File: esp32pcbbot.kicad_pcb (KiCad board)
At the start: 2 copper layers, 110 x 170 mm, 44 parts, among them IC1 BMI055, J1 TB002-500-02BE, J2 TB002-500-02BE, J3 TB002-500-02BE, J4 215299-4, J5 SSQ-120-01-L-D, J6 215299-4, Q1 2N7002, Q2 2N7002, Q3 Q_Photo_NPN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

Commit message: ...and i sized a voltage regulator incorrectly
...goshdangit here we go again autorouting...
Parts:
- VR2: value L78M05ABDT-TR -> L7905ACD2T-TR; footprint SamacSys_Parts:L78M05ABDTTR -> SamacSys_Parts:TO254P1542X460-3N
- moved J5 12.5 mm to (114.0, 64.5)
- moved S1 10.0 mm to (65.0, 74.0)
- moved S2 10.0 mm to (115.0, 74.0)
- moved S5 9.01 mm to (104.5, 70.0)
- moved J1 3.00 mm to (141.0, 51.0)
- moved J2 3.00 mm to (39.0, 56.0)
- moved J6 2.08 mm to (48.9, 75.0)
- moved VR1 1.52 mm to (107.2, 51.5)
- moved C4 1.50 mm to (130.0, 36.5)
- moved J3 1.50 mm to (107.0, 27.5)
- moved C7 1.41 mm to (117.0, 51.0)
- moved C8 1.00 mm to (130.0, 51.0)
- moved VR2 0.67 mm to (115.0, 38.0), turned to 0 degrees
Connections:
- VR2 pad 1: VCC -> GND
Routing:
- net GND: track 593.8 -> 0.00 mm, vias 1 -> 0
- net +5V: track 347.6 -> 0.00 mm, vias 2 -> 0
- net +3V3: track 214.9 -> 0.00 mm, vias 5 -> 0
- net 10Y: track 173.0 -> 0.00 mm, vias 1 -> 0
- net 12Y: track 150.6 -> 0.00 mm, vias 2 -> 0
- net 11Y: track 142.3 -> 0.00 mm
- net BOOT: track 137.3 -> 0.00 mm, vias 2 -> 0
- net VBUS: track 134.7 -> 0.00 mm, vias 4 -> 0
- net 7A: track 124.9 -> 0.00 mm, vias 3 -> 0
- net EN: track 124.5 -> 0.00 mm, vias 3 -> 0
- net 9Y: track 113.6 -> 0.00 mm
- net M1A: track 107.6 -> 0.00 mm
- net Net-(S2-Pad2): track 106.6 -> 0.00 mm, vias 1 -> 0
- net Net-(J5-Pad15): track 103.4 -> 0.00 mm, vias 2 -> 0
- net 10A: track 98.5 -> 0.00 mm, vias 5 -> 0
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
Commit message: work pls work pls i beg u to finally work
the ground thingy has been updated
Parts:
- moved C7 1.41 mm to (118.0, 52.0)
- moved C8 1.00 mm to (130.0, 52.0)
- moved VR2 1.00 mm to (115.0, 39.0)
- moved C4 0.50 mm to (130.0, 37.0)
- moved J3 0.50 mm to (107.0, 28.0)

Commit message: more autorouting shenanigins
please work i beg you pleaseworkpleaseworkpleasworkpleasework
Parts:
- moved Q1 5.39 mm to (61.0, 35.0)
- moved R4 4.47 mm to (61.0, 32.0)
- moved R3 3.75 mm to (60.8, 38.0)
- moved Q2 3.16 mm to (61.0, 41.0)
- moved U2 3.13 mm to (71.0, 39.9)
- moved R1 1.41 mm to (61.0, 30.0), turned to 180 degrees
- moved C3 1.00 mm to (50.0, 37.0)
- moved C5 1.00 mm to (50.0, 52.0)
- moved C6 1.00 mm to (62.0, 52.0)
- moved R2 1.00 mm to (61.0, 28.0), turned to 0 degrees
- moved USB1 1.00 mm to (71.0, 27.5)
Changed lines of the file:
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@@
   )
   (module SamacSys_Parts:EEEFK1V331P (layer F.Cu)
-    (at 62 51 180)
+    (at 62 52 180)
     (descr G)
     (tags "Capacitor Polarised")
@@
   )
   (module SamacSys_Parts:EEEFK1V331P (layer F.Cu)
-    (at 50 51 180)
+    (at 50 52 180)
     (descr G)
     (tags "Capacitor Polarised")
@@
   )
   (module SamacSys_Parts:EEEFK1V331P (layer F.Cu)
-    (at 50 36 180)
+    (at 50 37 180)
     (descr G)
     (tags "Capacitor Polarised")
@@
   )
   (module ESP32bot:USB_C_Receptacle_HRO_TYPE-C-31-M-12 (layer F.Cu)
-    (at 70 27.5 180)
+    (at 71 27.5 180)
     (descr "USB Type-C receptacle for USB 2.0 and PD, http://www.krhro.com/uploads/soft/180320/1-1P320120243.pdf")
     (tags "usb usb-c 2.0 pd")
@@
   )
   (module Package_DFN_QFN:QFN-28-1EP_5x5mm_P0.5mm_EP3.35x3.35mm (layer F.Cu)
-    (at 74 39 270)
+    (at 71 39.88 270)
     (descr "QFN, 28 Pin (http://ww1.microchip.com/downloads/en/PackagingSpec/00000049BQ.pdf#page=283), generated with kicad-footprint-generator ipc_noLead_generator.py")
     (tags "QFN NoLead")
@@
   )
   (module Resistor_SMD:R_0603_1608Metric (layer F.Cu)
-    (at 59 36)
+    (at 61 32)
     (descr "Resistor SMD 0603 (1608 Metric), square (rectangular) end terminal, IPC_7351 nominal, (Body size source: IPC-SM-782 page 72, https://www.pcb-3d.com/wordpress/wp-content/uploads/ipc-sm-782a_amendment_1_and_2.pdf), generated with kicad-footprint-generator")
     (tags resistor)
@@
   )
   (module Resistor_SMD:R_0603_1608Metric (layer F.Cu)
-    (at 64 36 180)
+    (at 60.825 38 180)
     (descr "Resistor SMD 0603 (1608 Metric), square (rectangular) end terminal, IPC_7351 nominal, (Body size source: IPC-SM-782 page 72, https://www.pcb-3d.com/wordpress/wp-content/uploads/ipc-sm-782a_amendment_1_and_2.pdf), generated with kicad-footprint-generator")
     (tags resistor)
@@
   )
   (module Resistor_SMD:R_0603_1608Metric (layer F.Cu)
-    (at 62 28 270)
+    (at 61 28)
     (descr "Resistor SMD 0603 (1608 Metric), square (rectangular) end terminal, IPC_7351 nominal, (Body size source: IPC-SM-782 page 72, https://www.pcb-3d.com/wordpress/wp-content/uploads/ipc-sm-782a_amendment_1_and_2.pdf), generated with kicad-footprint-generator")
     (tags resistor)
     (attr smd)
-    (fp_text reference R2 (at 0 -1 90) (layer F.SilkS)
-      (effects (font (size 1 1) (thickness 0.15)))
-    )
-    (fp_text value 5.11k (at 0 1.43 90) (layer F.Fab)
+    (fp_text reference R2 (at 0 -1) (layer F.SilkS)
+      (effects (font (size 1 1) (thickness 0.15)))
+    )
+    (fp_text value 5.11k (at 0 1.43) (layer F.Fab)
       (effects (font (size 1 1) (thickness 0.15)))
     )
@@
     (fp_line (start 1.48 -0.73) (end 1.48 0.73) (layer F.CrtYd) (width 0.05))
     (fp_line (start 1.48 0.73) (end -1.48 0.73) (layer F.CrtYd) (width 0.05))
-    (fp_text user %R (at -1 -1 90) (layer F.Fab)
+    (fp_text user %R (at -1 -1) (layer F.Fab)
       (effects (font (size 0.4 0.4) (thickness 0.06)))
     )
-    (pad 2 smd roundrect (at 0.825 0 270) (size 0.8 0.95) (layers F.Cu F.Paste F.Mask) (roundrect_rratio 0.25)
-      (net 2 GND))
-    (pad 1 smd roundrect (at -0.825 0 270) (size 0.8 0.95) (layers F.Cu F.Paste F.Mask) (roundrect_rratio 0.25)
+    (pad 2 smd roundrect (at 0.825 0) (size 0.8 0.95) (layers F.Cu F.Paste F.Mask) (roundrect_rratio 0.25)
+      (net 2 GND))
+    (pad 1 smd roundrect (at -0.825 0) (size 0.8 0.95) (layers F.Cu F.Paste F.Mask) (roundrect_rratio 0.25)
       (net 58 "Net-(R2-Pad1)"))
     (model ${KISYS3DMOD}/Resistor_SMD.3dshapes/R_0603_1608Metric.wrl
@@
   )
   (module Resistor_SMD:R_0603_1608Metric (layer F.Cu)
-    (at 62 31 90)
+    (at 61 30 180)
     (descr "Resistor SMD 0603 (1608 Metric), square (rectangular) end terminal, IPC_7351 nominal, (Body size source: IPC-SM-782 page 72, https://www.pcb-3d.com/wordpress/wp-content/uploads/ipc-sm-782a_amendment_1_and_2.pdf), generated with kicad-footprint-generator")
     (tags resistor)
     (attr smd)
-    (fp_text reference R1 (at 0 -1.43 90) (layer F.SilkS)
-      (effects (font (size 1 1) (thickness 0.15)))
-    )
-    (fp_text value 5.11k (at 0 1.43 90) (layer F.Fab)
+    (fp_text reference R1 (at 0 -1.43) (layer F.SilkS)
+      (effects (font (size 1 1) (thickness 0.15)))
+    )
+    (fp_text value 5.11k (at 0 1.43) (layer F.Fab)
       (effects (font (size 1 1) (thickness 0.15)))
     )
@@
     (fp_line (start 1.48 -0.73) (end 1.48 0.73) (layer F.CrtYd) (width 0.05))
     (fp_line (start 1.48 0.73) (end -1.48 0.73) (layer F.CrtYd) (width 0.05))
-    (fp_text user %R (at 0 0 180) (layer F.Fab)
+    (fp_text user %R (at 0 0 270) (layer F.Fab)
       (effects (font (size 0.4 0.4) (thickness 0.06)))
     )
-    (pad 2 smd roundrect (at 0.825 0 90) (size 0.8 0.95) (layers F.Cu F.Paste F.Mask) (roundrect_rratio 0.25)
-      (net 2 GND))
-    (pad 1 smd roundrect (at -0.825 0 90) (size 0.8 0.95) (layers F.Cu F.Paste F.Mask) (roundrect_rratio 0.25)
+    (pad 2 smd roundrect (at 0.825 0 180) (size 0.8 0.95) (layers F.Cu F.Paste F.Mask) (roundrect_rratio 0.25)
+      (net 2 GND))
+    (pad 1 smd roundrect (at -0.825 0 180) (size 0.8 0.95) (layers F.Cu F.Paste F.Mask) (roundrect_rratio 0.25)
       (net 57 "Net-(R1-Pad1)"))
     (model ${KISYS3DMOD}/Resistor_SMD.3dshapes/R_0603_1608Metric.wrl
@@
   )
   (module Package_TO_SOT_SMD:SOT-23 (layer F.Cu)
-    (at 64 40 270)
+    (at 61 41 270)
     (descr "SOT-23, Standard")
     (tags SOT-23)
@@
   )
   (module Package_TO_SOT_SMD:SOT-23 (layer F.Cu)
-    (at 59 40 270)
+    (at 61 35 270)
     (descr "SOT-23, Standard")
     (tags SOT-23)

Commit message: routing more
please work
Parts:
- moved Q1 2.24 mm to (59.0, 36.0)
- moved Q2 2.24 mm to (59.0, 42.0)
- moved R1 2.24 mm to (59.0, 31.0)
- moved R2 2.24 mm to (59.0, 29.0)
- moved R3 2.24 mm to (58.8, 39.0)
- moved R4 2.24 mm to (59.0, 33.0)
- moved USB1 2.00 mm to (69.0, 27.5)
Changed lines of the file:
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@@
   )
   (module ESP32bot:USB_C_Receptacle_HRO_TYPE-C-31-M-12 (layer F.Cu)
-    (at 71 27.5 180)
+    (at 69 27.5 180)
     (descr "USB Type-C receptacle for USB 2.0 and PD, http://www.krhro.com/uploads/soft/180320/1-1P320120243.pdf")
     (tags "usb usb-c 2.0 pd")
@@
   )
   (module Resistor_SMD:R_0603_1608Metric (layer F.Cu)
-    (at 61 32)
+    (at 59 33)
     (descr "Resistor SMD 0603 (1608 Metric), square (rectangular) end terminal, IPC_7351 nominal, (Body size source: IPC-SM-782 page 72, https://www.pcb-3d.com/wordpress/wp-content/uploads/ipc-sm-782a_amendment_1_and_2.pdf), generated with kicad-footprint-generator")
     (tags resistor)
@@
   )
   (module Resistor_SMD:R_0603_1608Metric (layer F.Cu)
-    (at 60.825 38 180)
+    (at 58.825 39 180)
     (descr "Resistor SMD 0603 (1608 Metric), square (rectangular) end terminal, IPC_7351 nominal, (Body size source: IPC-SM-782 page 72, https://www.pcb-3d.com/wordpress/wp-content/uploads/ipc-sm-782a_amendment_1_and_2.pdf), generated with kicad-footprint-generator")
     (tags resistor)
@@
   )
   (module Resistor_SMD:R_0603_1608Metric (layer F.Cu)
-    (at 61 28)
+    (at 59 29)
     (descr "Resistor SMD 0603 (1608 Metric), square (rectangular) end terminal, IPC_7351 nominal, (Body size source: IPC-SM-782 page 72, https://www.pcb-3d.com/wordpress/wp-content/uploads/ipc-sm-782a_amendment_1_and_2.pdf), generated with kicad-footprint-generator")
     (tags resistor)
@@
   )
   (module Resistor_SMD:R_0603_1608Metric (layer F.Cu)
-    (at 61 30 180)
+    (at 59 31 180)
     (descr "Resistor SMD 0603 (1608 Metric), square (rectangular) end terminal, IPC_7351 nominal, (Body size source: IPC-SM-782 page 72, https://www.pcb-3d.com/wordpress/wp-content/uploads/ipc-sm-782a_amendment_1_and_2.pdf), generated with kicad-footprint-generator")
     (tags resistor)
@@
   )
   (module Package_TO_SOT_SMD:SOT-23 (layer F.Cu)
-    (at 61 41 270)
+    (at 59 42 270)
     (descr "SOT-23, Standard")
     (tags SOT-23)
@@
   )
   (module Package_TO_SOT_SMD:SOT-23 (layer F.Cu)
-    (at 61 35 270)
+    (at 59 36 270)
     (descr "SOT-23, Standard")
     (tags SOT-23)

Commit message: more autorouting
lets hope this works
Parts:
- moved Q1 16.6 mm to (74.0, 43.0)
- moved Q2 16.6 mm to (74.0, 49.0)
- moved R3 16.6 mm to (73.8, 46.0)
- moved R4 16.6 mm to (74.0, 40.0)
- moved U2 6.29 mm to (65.0, 38.0)
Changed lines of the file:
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@@
   )
   (module Package_DFN_QFN:QFN-28-1EP_5x5mm_P0.5mm_EP3.35x3.35mm (layer F.Cu)
-    (at 71 39.88 270)
+    (at 65 38 270)
     (descr "QFN, 28 Pin (http://ww1.microchip.com/downloads/en/PackagingSpec/00000049BQ.pdf#page=283), generated with kicad-footprint-generator ipc_noLead_generator.py")
     (tags "QFN NoLead")
@@
   )
   (module Resistor_SMD:R_0603_1608Metric (layer F.Cu)
-    (at 59 33)
+    (at 74 40)
     (descr "Resistor SMD 0603 (1608 Metric), square (rectangular) end terminal, IPC_7351 nominal, (Body size source: IPC-SM-782 page 72, https://www.pcb-3d.com/wordpress/wp-content/uploads/ipc-sm-782a_amendment_1_and_2.pdf), generated with kicad-footprint-generator")
     (tags resistor)
@@
   )
   (module Resistor_SMD:R_0603_1608Metric (layer F.Cu)
-    (at 58.825 39 180)
+    (at 73.825 46 180)
     (descr "Resistor SMD 0603 (1608 Metric), square (rectangular) end terminal, IPC_7351 nominal, (Body size source: IPC-SM-782 page 72, https://www.pcb-3d.com/wordpress/wp-content/uploads/ipc-sm-782a_amendment_1_and_2.pdf), generated with kicad-footprint-generator")
     (tags resistor)
@@
   )
   (module Package_TO_SOT_SMD:SOT-23 (layer F.Cu)
-    (at 59 42 270)
+    (at 74 49 270)
     (descr "SOT-23, Standard")
     (tags SOT-23)
@@
   )
   (module Package_TO_SOT_SMD:SOT-23 (layer F.Cu)
-    (at 59 36 270)
+    (at 74 43 270)
     (descr "SOT-23, Standard")
     (tags SOT-23)

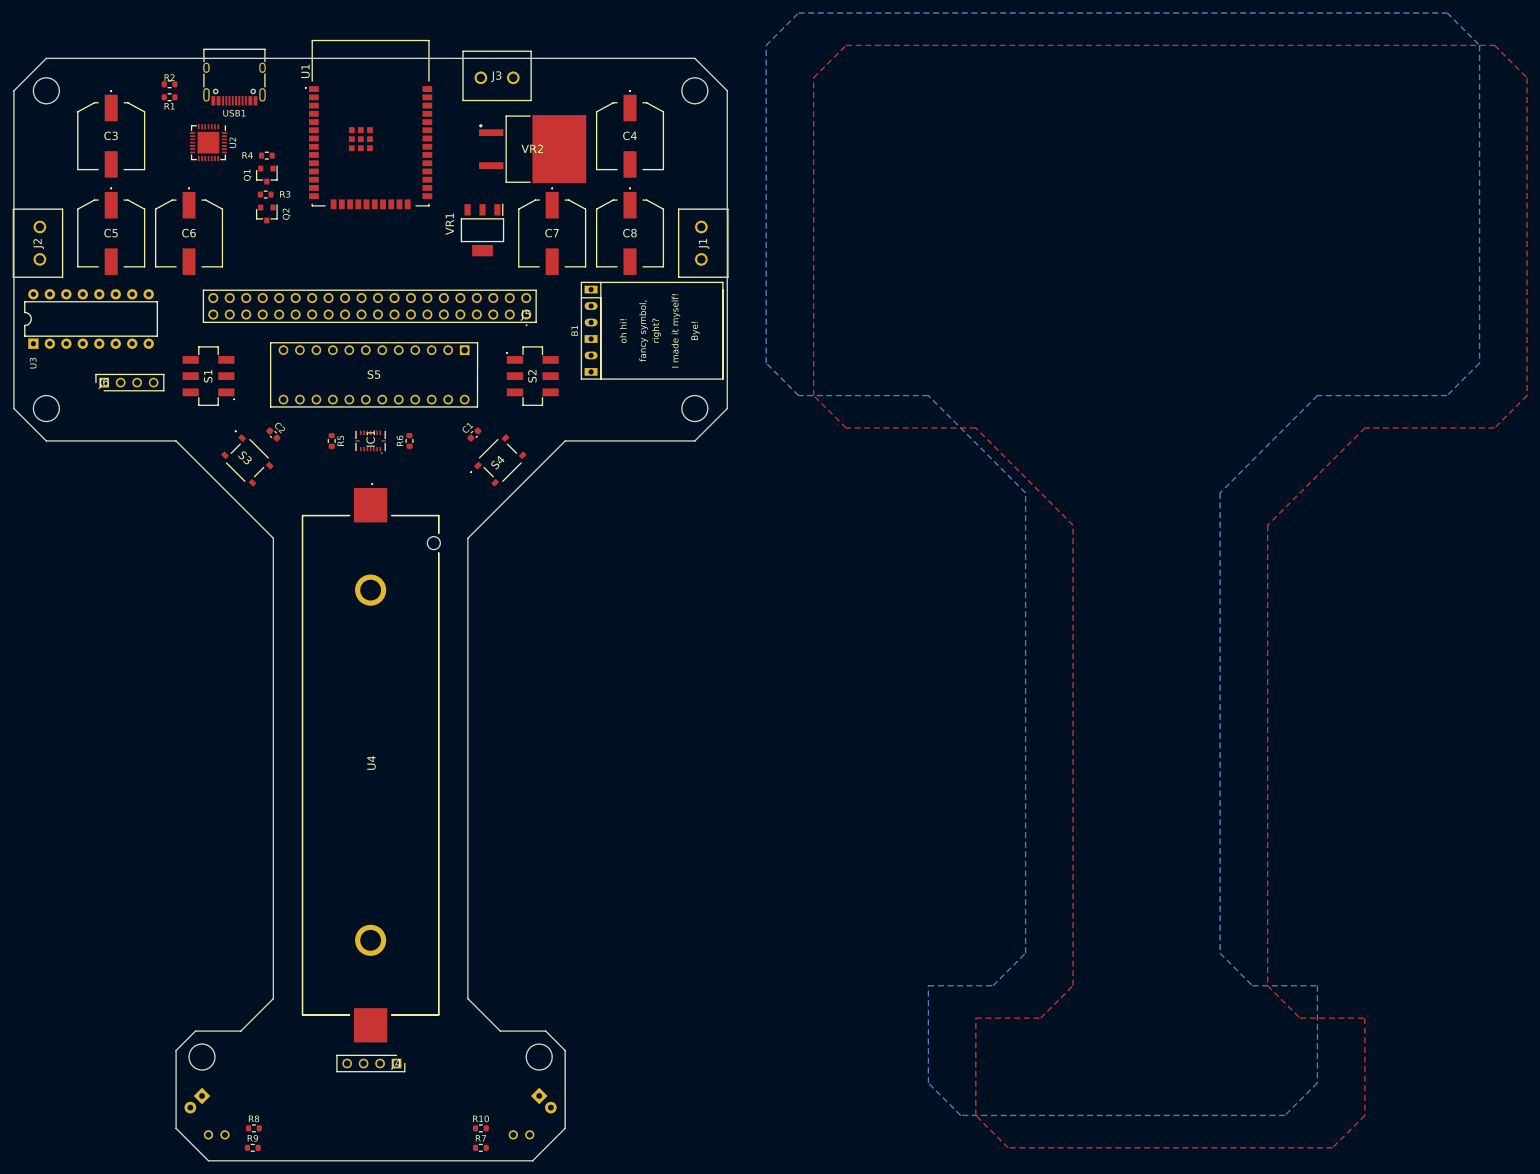
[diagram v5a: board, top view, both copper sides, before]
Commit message: more autorouting
user error last time, lets hope this one works
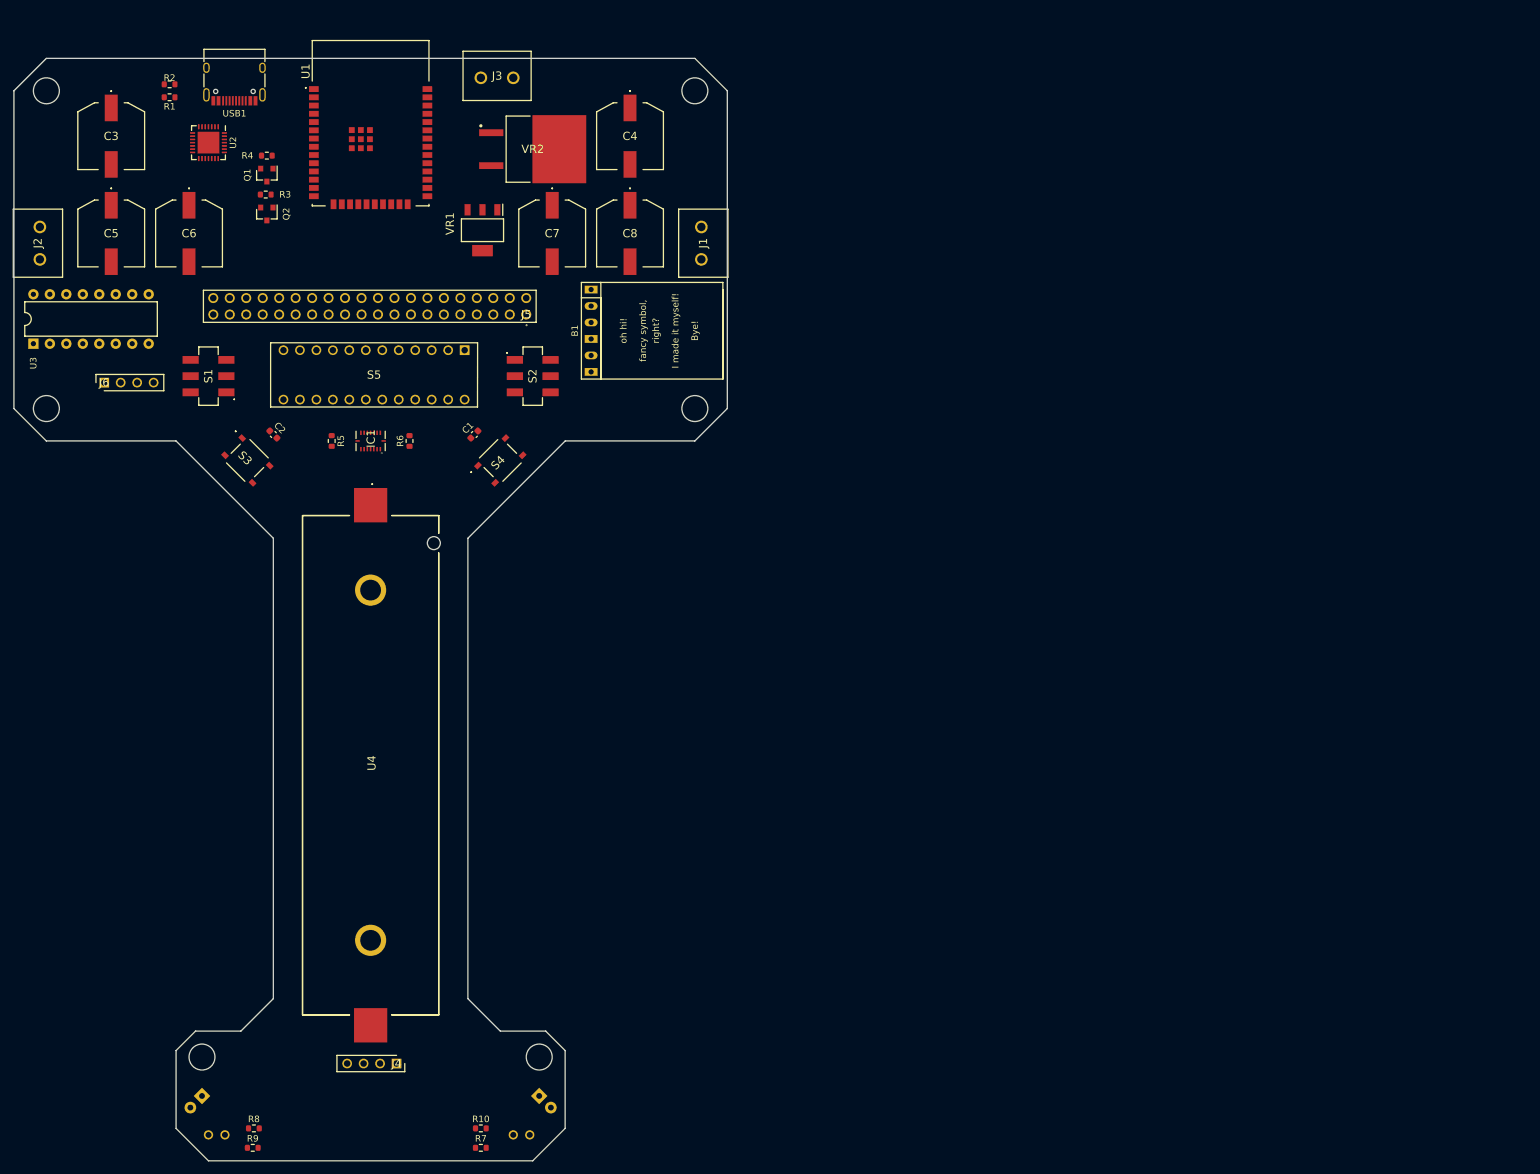
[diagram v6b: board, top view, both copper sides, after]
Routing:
- removed copper zone on B.Cu, net GND
- removed copper zone on F.Cu, net GND
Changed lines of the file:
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@@
-    )
-  )
-  (zone (net 2) (net_name GND) (layer F.Cu) (hatch edge 0.508)
-    (connect_pads (clearance 0.508))
-    (min_thickness 0.254)
-    (fill yes (arc_segments 32) (thermal_gap 0.508) (thermal_bridge_width 0.508))
-    (polygon
-      (pts
-        (xy 268.322887 28) (xy 268.322887 77) (xy 263.322887 82) (xy 243.322887 82) (xy 228.322887 97)
-        (xy 228.322887 168) (xy 233.322887 173) (xy 243.322887 173) (xy 243.322887 188) (xy 238.322887 193)
-        (xy 188.322887 193) (xy 183.322887 188) (xy 183.322887 173) (xy 193.322887 173) (xy 198.322887 168)
-        (xy 198.322887 97) (xy 183.322887 82) (xy 163.322887 82) (xy 158.322887 77) (xy 158.322887 28)
-        (xy 163.322887 23) (xy 263.322887 23)
-      )
-    )
-  )
-  (zone (net 2) (net_name GND) (layer B.Cu) (hatch edge 0.508)
-    (connect_pads (clearance 0.508))
-    (min_thickness 0.254)
-    (fill yes (arc_segments 32) (thermal_gap 0.508) (thermal_bridge_width 0.508))
-    (polygon
-      (pts
-        (xy 261 23) (xy 261 72) (xy 256 77) (xy 236 77) (xy 221 92)
-        (xy 221 163) (xy 226 168) (xy 236 168) (xy 236 183) (xy 231 188)
-        (xy 181 188) (xy 176 183) (xy 176 168) (xy 186 168) (xy 191 163)
-        (xy 191 92) (xy 176 77) (xy 156 77) (xy 151 72) (xy 151 23)
-        (xy 156 18) (xy 256 18)
-      )
     )
   )

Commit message: more autorouting
horay hora
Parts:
- turned R2 to 180 degrees
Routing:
- added copper zone on F.Cu, net GND
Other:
- net class Power: trace_width 0.5 -> 0.8
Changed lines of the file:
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@@
   (net_class Power ""
     (clearance 0.2)
-    (trace_width 0.5)
+    (trace_width 0.8)
     (via_dia 1)
     (via_drill 0.5)
@@
   )
   (module Resistor_SMD:R_0603_1608Metric (layer F.Cu)
-    (at 59 29)
+    (at 59 29 180)
     (descr "Resistor SMD 0603 (1608 Metric), square (rectangular) end terminal, IPC_7351 nominal, (Body size source: IPC-SM-782 page 72, https://www.pcb-3d.com/wordpress/wp-content/uploads/ipc-sm-782a_amendment_1_and_2.pdf), generated with kicad-footprint-generator")
     (tags resistor)
     (attr smd)
-    (fp_text reference R2 (at 0 -1) (layer F.SilkS)
+    (fp_text reference R2 (at 0 2) (layer F.SilkS)
       (effects (font (size 1 1) (thickness 0.15)))
     )
@@
       (effects (font (size 0.4 0.4) (thickness 0.06)))
     )
-    (pad 2 smd roundrect (at 0.825 0) (size 0.8 0.95) (layers F.Cu F.Paste F.Mask) (roundrect_rratio 0.25)
-      (net 2 GND))
-    (pad 1 smd roundrect (at -0.825 0) (size 0.8 0.95) (layers F.Cu F.Paste F.Mask) (roundrect_rratio 0.25)
+    (pad 2 smd roundrect (at 0.825 0 180) (size 0.8 0.95) (layers F.Cu F.Paste F.Mask) (roundrect_rratio 0.25)
+      (net 2 GND))
+    (pad 1 smd roundrect (at -0.825 0 180) (size 0.8 0.95) (layers F.Cu F.Paste F.Mask) (roundrect_rratio 0.25)
       (net 58 "Net-(R2-Pad1)"))
     (model ${KISYS3DMOD}/Resistor_SMD.3dshapes/R_0603_1608Metric.wrl
@@
       )
     )
+  )
+  (zone (net 2) (net_name GND) (layer F.Cu) (hatch edge 0.508)
+    (connect_pads (clearance 0.508))
+    (min_thickness 0.254)
+    (fill yes (arc_segments 32) (thermal_gap 0.508) (thermal_bridge_width 0.508))
+    (polygon
+      (pts
+        (xy 80 54) (xy 69 54) (xy 69 42) (xy 57 42) (xy 57 25)
+        (xy 80 25)
+      )
+    )
